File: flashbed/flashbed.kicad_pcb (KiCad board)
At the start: 2 copper layers, 63.5 x 59.7 mm, 47 parts, among them J1 , J2 , J3 , J4 , SW1 SW_Push

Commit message: Cập nhật file PCB
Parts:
- added kibuzzard-62E56558: G***, kibuzzard-62E56558, F.Cu at (81.9, 29.2)
- J4: footprint Connector_IDC:IDC-Header_2x05_P2.54mm_Vertical -> Connector_IDC:IDC-Header_2x05_P2.54mm_Horizontal
- moved J4 10.9 mm to (87.6, 71.1), turned to -90 degrees
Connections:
- J2 pad 4: Net-(J2-Pad4) -> RST
- J4 pad 1: unconnected-(J4-Pad1) -> RST
- SW1 pad 2: Net-(J2-Pad4) -> RST
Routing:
- net RST: track 0.00 -> 42.6 mm
- net Net-(J2-Pad4): track 12.3 -> 0.00 mm
- net SWDIO: track 19.7 -> 22.9 mm
- net SWCLK: track 17.8 -> 21.0 mm
- net +3V3: track 25.0 -> 23.7 mm
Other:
- board text added: "Bat+"
- board text added: "Bat-"
- board text removed: "-"
- board text removed: "B+"

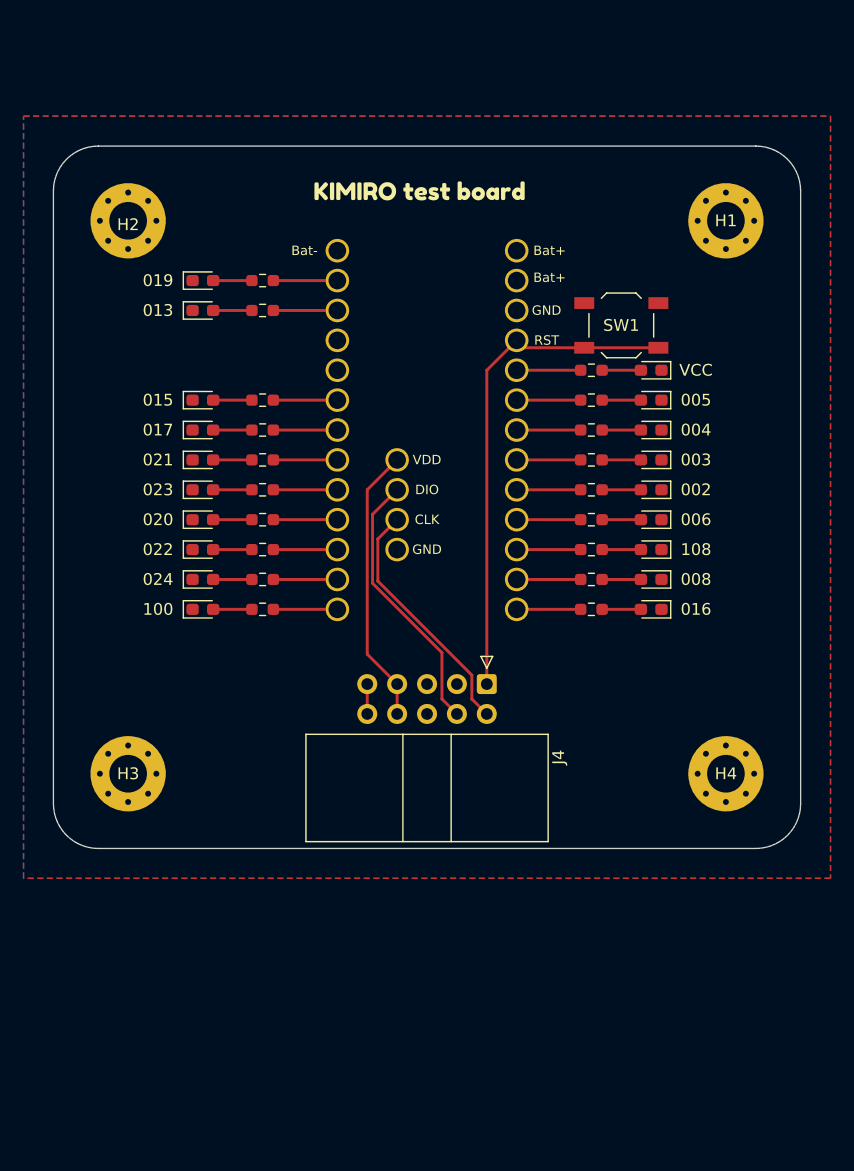
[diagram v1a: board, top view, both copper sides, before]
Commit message: Cập nhật: - Thêm flashbed cho nrfpill - Thay đổi GPIO Kimiro
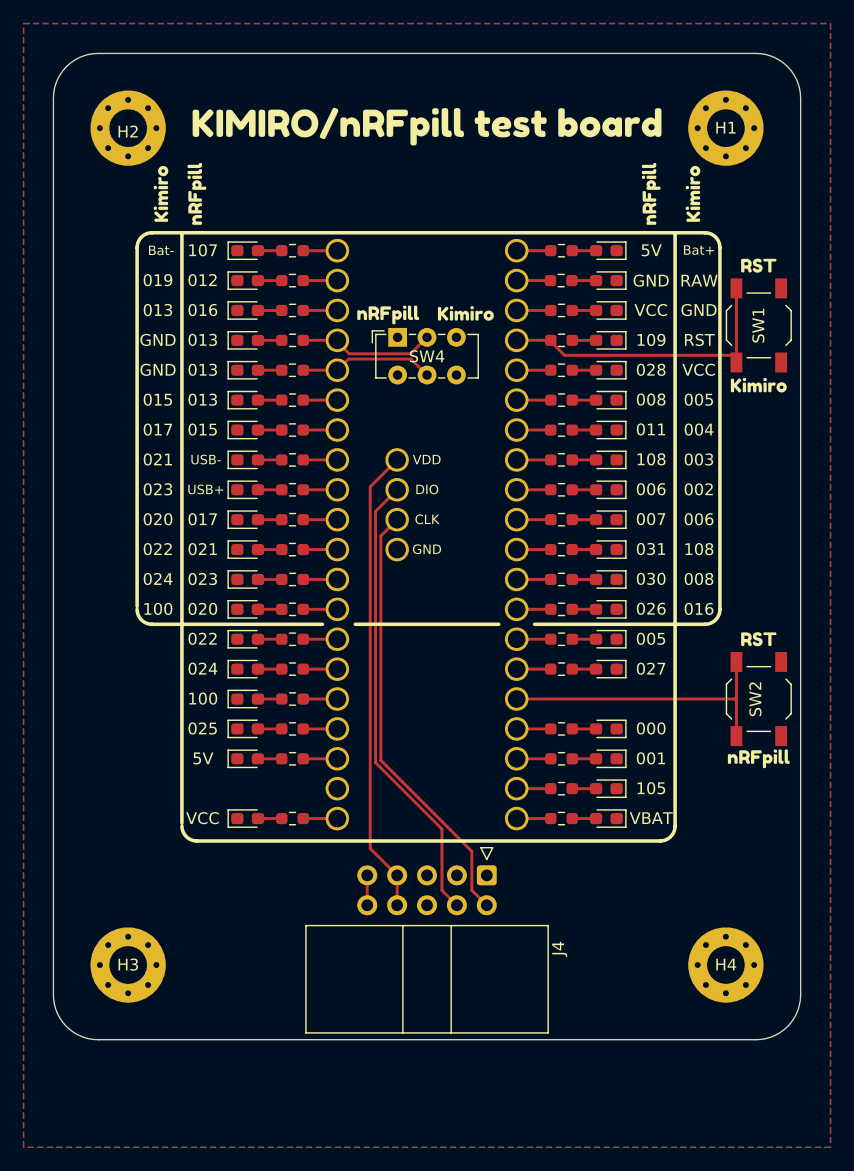
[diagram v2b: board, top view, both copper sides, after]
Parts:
- removed J1, J2: , Library:PinHeader_1x13_P2.54mm_Vertical
- removed kibuzzard-62E56558: G***, kibuzzard-62E56558
- added D1: 5V, Library:LED_0603_1608Metric_Pad1.05x0.95mm_HandSolder, F.Cu at (97.8, 34.3)
- added D2: 5V, Library:LED_0603_1608Metric_Pad1.05x0.95mm_HandSolder, F.Cu at (67.3, 77.5)
- added D27: 013, Library:LED_0603_1608Metric_Pad1.05x0.95mm_HandSolder, F.Cu at (67.3, 44.5)
- added D28: 022, Library:LED_0603_1608Metric_Pad1.05x0.95mm_HandSolder, F.Cu at (67.3, 67.3)
- added D29: 024, Library:LED_0603_1608Metric_Pad1.05x0.95mm_HandSolder, F.Cu at (67.3, 69.8)
- added D30: 100, Library:LED_0603_1608Metric_Pad1.05x0.95mm_HandSolder, F.Cu at (67.3, 72.4)
- added D31: 025, Library:LED_0603_1608Metric_Pad1.05x0.95mm_HandSolder, F.Cu at (67.3, 74.9)
- added D32: 005, Library:LED_0603_1608Metric_Pad1.05x0.95mm_HandSolder, F.Cu at (97.8, 67.3)
- added D33: 027, Library:LED_0603_1608Metric_Pad1.05x0.95mm_HandSolder, F.Cu at (97.8, 69.8)
- added D34: 000, Library:LED_0603_1608Metric_Pad1.05x0.95mm_HandSolder, F.Cu at (97.8, 74.9)
- added D35: 001, Library:LED_0603_1608Metric_Pad1.05x0.95mm_HandSolder, F.Cu at (97.8, 77.5)
- added D36: 105, Library:LED_0603_1608Metric_Pad1.05x0.95mm_HandSolder, F.Cu at (97.8, 80.0)
- added D37: VBAT, Library:LED_0603_1608Metric_Pad1.05x0.95mm_HandSolder, F.Cu at (97.8, 82.5)
- added D38: RAW, Library:LED_0603_1608Metric_Pad1.05x0.95mm_HandSolder, F.Cu at (97.8, 36.8)
- added D4: VCC, Library:LED_0603_1608Metric_Pad1.05x0.95mm_HandSolder, F.Cu at (67.3, 82.5)
- added D6: VCC, Library:LED_0603_1608Metric_Pad1.05x0.95mm_HandSolder, F.Cu at (97.8, 39.4)
- added D7: 109, Library:LED_0603_1608Metric_Pad1.05x0.95mm_HandSolder, F.Cu at (97.8, 41.9)
- added D8: 107, Library:LED_0603_1608Metric_Pad1.05x0.95mm_HandSolder, F.Cu at (67.3, 34.3)
- added D9: 013, Library:LED_0603_1608Metric_Pad1.05x0.95mm_HandSolder, F.Cu at (67.3, 41.9)
- added J5: Conn_01x20, Library:PinHeader_1x20_P2.54mm_Vertical, F.Cu at (74.9, 34.3)
- added J6: Conn_01x20, Library:PinHeader_1x20_P2.54mm_Vertical, F.Cu at (90.2, 34.3)
- added R1: 10k, Library:R_0603_1608Metric_Pad0.98x0.95mm_HandSolder, F.Cu at (71.1, 34.3)
- added R2: 10k, Library:R_0603_1608Metric_Pad0.98x0.95mm_HandSolder, F.Cu at (71.1, 41.9)
- added R27: 10k, Library:R_0603_1608Metric_Pad0.98x0.95mm_HandSolder, F.Cu at (71.1, 72.4)
- added R28: 10k, Library:R_0603_1608Metric_Pad0.98x0.95mm_HandSolder, F.Cu at (71.1, 74.9)
- added R29: 10k, Library:R_0603_1608Metric_Pad0.98x0.95mm_HandSolder, F.Cu at (94.0, 74.9)
- added R30: 10k, Library:R_0603_1608Metric_Pad0.98x0.95mm_HandSolder, F.Cu at (71.1, 77.5)
- added R31: 10k, Library:R_0603_1608Metric_Pad0.98x0.95mm_HandSolder, F.Cu at (94.0, 77.5)
- added R32: 10k, Library:R_0603_1608Metric_Pad0.98x0.95mm_HandSolder, F.Cu at (94.0, 36.8)
- added R33: 10k, Library:R_0603_1608Metric_Pad0.98x0.95mm_HandSolder, F.Cu at (94.0, 80.0)
- added R34: 10k, Library:R_0603_1608Metric_Pad0.98x0.95mm_HandSolder, F.Cu at (71.1, 82.5)
- added R35: 10k, Library:R_0603_1608Metric_Pad0.98x0.95mm_HandSolder, F.Cu at (94.0, 82.5)
- added R36: 10k, Library:R_0603_1608Metric_Pad0.98x0.95mm_HandSolder, F.Cu at (94.0, 34.3)
- added R38: 10k, Library:R_0603_1608Metric_Pad0.98x0.95mm_HandSolder, F.Cu at (94.0, 39.4)
- added R39: 10k, Library:R_0603_1608Metric_Pad0.98x0.95mm_HandSolder, F.Cu at (94.0, 41.9)
- added R4: 10k, Library:R_0603_1608Metric_Pad0.98x0.95mm_HandSolder, F.Cu at (71.1, 44.5)
- added R6: 10k, Library:R_0603_1608Metric_Pad0.98x0.95mm_HandSolder, F.Cu at (71.1, 67.3)
- added R7: 10k, Library:R_0603_1608Metric_Pad0.98x0.95mm_HandSolder, F.Cu at (94.0, 67.3)
- added R8: 10k, Library:R_0603_1608Metric_Pad0.98x0.95mm_HandSolder, F.Cu at (71.1, 69.8)
- added R9: 10k, Library:R_0603_1608Metric_Pad0.98x0.95mm_HandSolder, F.Cu at (94.0, 69.8)
- added SW2: SW_Push, Button_Switch_SMD:SW_SPST_TL3342, F.Cu at (110.7, 72.4)
- added SW4: SW_DPDT_x2, Button_Switch_THT:SW_E-Switch_EG1271_DPDT, F.Cu at (80.0, 41.7)
- added kibuzzard-62E8B981: G***, kibuzzard-62E8B981, F.Cu at (101.6, 29.5)
- added kibuzzard-62E8B981: G***, kibuzzard-62E8B981, F.Cu at (63.0, 29.5)
- added kibuzzard-62E8B9A9: G***, kibuzzard-62E8B9A9, F.Cu at (105.2, 29.5)
- added kibuzzard-62E8B9A9: G***, kibuzzard-62E8B9A9, F.Cu at (59.9, 29.5)
- added kibuzzard-62E8BA68: G***, kibuzzard-62E8BA68, F.Cu at (110.7, 35.6)
- added kibuzzard-62E8BA68: G***, kibuzzard-62E8BA68, F.Cu at (110.7, 67.3)
- added kibuzzard-62E8BA80: G***, kibuzzard-62E8BA80, F.Cu at (110.7, 45.7)
- added kibuzzard-62E8BFC7: G***, kibuzzard-62E8BFC7, F.Cu at (110.7, 77.5)
- added kibuzzard-62E8C671: G***, kibuzzard-62E8C671, F.Cu at (85.9, 39.6)
- added kibuzzard-62E8C682: G***, kibuzzard-62E8C682, F.Cu at (79.2, 39.8)
- added kibuzzard-62E8CAF6: G***, kibuzzard-62E8CAF6, F.Cu at (82.5, 23.7)
- moved H3 16.3 mm to (57.1, 95.0)
- moved H4 16.3 mm to (108.0, 95.0)
- moved J4 16.3 mm to (87.6, 87.4)
- moved SW1 11.7 mm to (110.7, 40.6), turned to 90 degrees
- moved H1 7.87 mm to (108.0, 23.9)
- moved H2 7.87 mm to (57.1, 23.9)
- moved D11 3.81 mm to (67.3, 47.0)
- moved D13 3.81 mm to (67.3, 49.5)
- moved D15 3.81 mm to (67.3, 52.1)
- moved D17 3.81 mm to (67.3, 54.6)
- moved D19 3.81 mm to (67.3, 57.1)
- moved D21 3.81 mm to (67.3, 59.7)
- moved D23 3.81 mm to (67.3, 62.2)
- moved D25 3.81 mm to (67.3, 64.8)
- moved D3 3.81 mm to (67.3, 36.8)
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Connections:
- SW1 pad 1: GND -> RST_kimiro
- SW1 pad 2: RST -> GND
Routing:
- net RST: track 42.6 -> 0.00 mm
- net RST_kimiro: track 0.00 -> 25.9 mm
- net RST_nRFpill: track 0.00 -> 25.2 mm
- net SWCLK: track 21.0 -> 37.1 mm
- net SWDIO: track 22.9 -> 38.9 mm
- net +3V3: track 23.7 -> 39.7 mm
- net Net-(J5-Pad4): track 0.00 -> 11.6 mm
- net Net-(J5-Pad5): track 0.00 -> 11.5 mm
- net Net-(J5-Pad20): track 0.00 -> 2.90 mm
- net Net-(J5-Pad18): track 0.00 -> 2.90 mm
- net Net-(J5-Pad17): track 0.00 -> 2.90 mm
- net Net-(J5-Pad16): track 0.00 -> 2.90 mm
- net Net-(J5-Pad15): track 0.00 -> 2.90 mm
- net Net-(J5-Pad14): track 0.00 -> 2.90 mm
- net Net-(J5-Pad1): track 0.00 -> 2.90 mm
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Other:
- board size 63.5 x 59.7 mm -> 63.5 x 83.8 mm

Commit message: Cap nhat
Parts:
- added J2: , Library:PinHeader_1x04_P2.54mm_Vertical, F.Cu at (82.5, 72.4)
- added kibuzzard-62FFA6E2: G***, kibuzzard-62FFA6E2, F.Cu at (63.6, 34.3)
- added kibuzzard-62FFA7C6: G***, kibuzzard-62FFA7C6, F.Cu at (63.6, 36.8)
- added kibuzzard-62FFA7D6: G***, kibuzzard-62FFA7D6, F.Cu at (63.6, 39.4)
- added kibuzzard-62FFA7E0: G***, kibuzzard-62FFA7E0, F.Cu at (63.6, 41.9)
- added kibuzzard-62FFA7ED: G***, kibuzzard-62FFA7ED, F.Cu at (63.6, 44.5)
- added kibuzzard-62FFA7F8: G***, kibuzzard-62FFA7F8, F.Cu at (63.6, 47.0)
- added kibuzzard-62FFA800: G***, kibuzzard-62FFA800, F.Cu at (63.6, 49.5)
- added kibuzzard-62FFA80D: G***, kibuzzard-62FFA80D, F.Cu at (63.6, 52.1)
- added kibuzzard-62FFA814: G***, kibuzzard-62FFA814, F.Cu at (63.6, 54.6)
- added kibuzzard-62FFA81E: G***, kibuzzard-62FFA81E, F.Cu at (63.5, 57.1)
- added kibuzzard-62FFA82A: G***, kibuzzard-62FFA82A, F.Cu at (63.5, 59.7)
- added kibuzzard-62FFA831: G***, kibuzzard-62FFA831, F.Cu at (63.5, 62.2)
- added kibuzzard-62FFA83C: G***, kibuzzard-62FFA83C, F.Cu at (63.5, 64.8)
- added kibuzzard-62FFA843: G***, kibuzzard-62FFA843, F.Cu at (63.5, 67.3)
- added kibuzzard-62FFA850: G***, kibuzzard-62FFA850, F.Cu at (63.5, 69.8)
- added kibuzzard-62FFA857: G***, kibuzzard-62FFA857, F.Cu at (63.5, 72.4)
- added kibuzzard-62FFA865: G***, kibuzzard-62FFA865, F.Cu at (63.5, 74.9)
- added kibuzzard-62FFA86F: G***, kibuzzard-62FFA86F, F.Cu at (63.5, 77.5)
- added kibuzzard-62FFA878: G***, kibuzzard-62FFA878, F.Cu at (63.5, 82.5)
- added kibuzzard-62FFA8B7: G***, kibuzzard-62FFA8B7, F.Cu at (101.6, 34.3)
- added kibuzzard-62FFA8DA: G***, kibuzzard-62FFA8DA, F.Cu at (101.6, 41.9)
- added kibuzzard-62FFA8E6: G***, kibuzzard-62FFA8E6, F.Cu at (101.6, 44.5)
- added kibuzzard-62FFA8EF: G***, kibuzzard-62FFA8EF, F.Cu at (101.6, 47.0)
- added kibuzzard-62FFA8F8: G***, kibuzzard-62FFA8F8, F.Cu at (101.6, 49.5)
- added kibuzzard-62FFA905: G***, kibuzzard-62FFA905, F.Cu at (101.6, 52.1)
- added kibuzzard-62FFA912: G***, kibuzzard-62FFA912, F.Cu at (101.6, 54.6)
- added kibuzzard-62FFA91D: G***, kibuzzard-62FFA91D, F.Cu at (101.6, 57.1)
- added kibuzzard-62FFA928: G***, kibuzzard-62FFA928, F.Cu at (101.6, 59.7)
- added kibuzzard-62FFA93D: G***, kibuzzard-62FFA93D, F.Cu at (101.6, 62.2)
- added kibuzzard-62FFA945: G***, kibuzzard-62FFA945, F.Cu at (101.6, 64.8)
- added kibuzzard-62FFA950: G***, kibuzzard-62FFA950, F.Cu at (101.6, 67.3)
- added kibuzzard-62FFA95A: G***, kibuzzard-62FFA95A, F.Cu at (101.6, 69.8)
- added kibuzzard-62FFA971: G***, kibuzzard-62FFA971, F.Cu at (101.6, 74.9)
- added kibuzzard-62FFA976: G***, kibuzzard-62FFA976, F.Cu at (101.6, 77.5)
- added kibuzzard-62FFA982: G***, kibuzzard-62FFA982, F.Cu at (101.6, 80.0)
- added kibuzzard-62FFA9DB: G***, kibuzzard-62FFA9DB, F.Cu at (59.8, 36.8)
- added kibuzzard-62FFA9EA: G***, kibuzzard-62FFA9EA, F.Cu at (59.8, 39.4)
- added kibuzzard-62FFA9FF: G***, kibuzzard-62FFA9FF, F.Cu at (59.8, 44.5)
- added kibuzzard-62FFAA07: G***, kibuzzard-62FFAA07, F.Cu at (59.8, 41.9)
- added kibuzzard-62FFAA07: G***, kibuzzard-62FFAA07, F.Cu at (59.8, 34.3)
- added kibuzzard-62FFAA11: G***, kibuzzard-62FFAA11, F.Cu at (59.8, 47.0)
- added kibuzzard-62FFAA17: G***, kibuzzard-62FFAA17, F.Cu at (59.8, 49.5)
- added kibuzzard-62FFAA21: G***, kibuzzard-62FFAA21, F.Cu at (59.8, 52.1)
- added kibuzzard-62FFAA2C: G***, kibuzzard-62FFAA2C, F.Cu at (59.8, 54.6)
- added kibuzzard-62FFAA36: G***, kibuzzard-62FFAA36, F.Cu at (59.8, 57.1)
- added kibuzzard-62FFAA3C: G***, kibuzzard-62FFAA3C, F.Cu at (59.8, 59.7)
- added kibuzzard-62FFAA43: G***, kibuzzard-62FFAA43, F.Cu at (59.8, 62.2)
- added kibuzzard-62FFAA4B: G***, kibuzzard-62FFAA4B, F.Cu at (59.8, 64.8)
- added kibuzzard-62FFAA5B: G***, kibuzzard-62FFAA5B, F.Cu at (105.5, 36.8)
- added kibuzzard-62FFAA5B: G***, kibuzzard-62FFAA5B, F.Cu at (105.5, 34.3)
- added kibuzzard-62FFAA62: G***, kibuzzard-62FFAA62, F.Cu at (101.6, 36.8)
- added kibuzzard-62FFAA68: G***, kibuzzard-62FFAA68, F.Cu at (101.6, 39.4)
- added kibuzzard-62FFAA85: G***, kibuzzard-62FFAA85, F.Cu at (105.5, 39.4)
- added kibuzzard-62FFAA92: G***, kibuzzard-62FFAA92, F.Cu at (105.5, 41.9)
- added kibuzzard-62FFAA9F: G***, kibuzzard-62FFAA9F, F.Cu at (105.5, 44.5)
- added kibuzzard-62FFAAAB: G***, kibuzzard-62FFAAAB, F.Cu at (105.5, 47.0)
- added kibuzzard-62FFAAB5: G***, kibuzzard-62FFAAB5, F.Cu at (105.5, 49.5)
- added kibuzzard-62FFAAC5: G***, kibuzzard-62FFAAC5, F.Cu at (105.5, 52.1)
- added kibuzzard-62FFAACE: G***, kibuzzard-62FFAACE, F.Cu at (105.5, 54.6)
- added kibuzzard-62FFAAD6: G***, kibuzzard-62FFAAD6, F.Cu at (105.5, 57.1)
- added kibuzzard-62FFAAE1: G***, kibuzzard-62FFAAE1, F.Cu at (105.5, 59.7)
- added kibuzzard-62FFAAE6: G***, kibuzzard-62FFAAE6, F.Cu at (105.5, 62.2)
- added kibuzzard-62FFAAEE: G***, kibuzzard-62FFAAEE, F.Cu at (105.5, 64.8)
- added kibuzzard-62FFAB1C: G***, kibuzzard-62FFAB1C, F.Cu at (101.6, 72.4)
- added kibuzzard-62FFAB24: G***, kibuzzard-62FFAB24, F.Cu at (101.6, 82.5)
- added kibuzzard-62FFAB5E: G***, kibuzzard-62FFAB5E, F.Cu at (85.1, 74.9)
- added kibuzzard-62FFAB6D: G***, kibuzzard-62FFAB6D, F.Cu at (85.1, 77.5)
- moved kibuzzard-62E8B981 0.64 mm to (63.6, 29.5)
- moved kibuzzard-62E8B9A9 0.25 mm to (105.4, 29.5)
- moved kibuzzard-62E8B9A9 0.13 mm to (59.8, 29.5)
- renumbered D8 to D1, D1 to D2, D28 to D27, D32 to D28, D33 to D30, D30 to D31, D31 to D32, D34 to D33, D2 to D34, D4 to D37, D37 to D38, D38 to D4, D9 to D7, D7 to D8, D27 to D9, J3 to J1, J5 to J3, J6 to J4, J4 to J5, R36 to R2, R6 to R27, R7 to R28, R8 to R29, R9 to R30, R27 to R31, R28 to R32, R29 to R33, R30 to R34, R31 to R35, R33 to R36, R34 to R37, R35 to R38, R32 to R4, R38 to R6, R2 to R7, R39 to R8, R4 to R9, SW4 to SW1, SW1 to SW2, SW2 to SW3
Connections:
- J3 pad 18: Net-(J5-Pad18) -> +5V
- R34 pad 1: Net-(J5-Pad18) -> +5V
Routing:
- net +5V: track 2.54 -> 16.3 mm
- net Net-(J5-Pad18): track 2.90 -> 0.00 mm
- net +3V3: track 39.7 -> 39.2 mm
- net GND: vias 0 -> 1
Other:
- board text removed: "Bat+"
- board text removed: "Bat-"
- board text removed: "RST"
